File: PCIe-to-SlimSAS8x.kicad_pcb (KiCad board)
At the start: 4 copper layers, 27.3 x 51.3 mm, 11 parts, among them J1 PCI_Express_x8, J2 OpenCAPI_AAC_Host

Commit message: Initial Layout Complete
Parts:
- renumbered R4 to R3, R3 to R4
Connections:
- net PERn0 renamed Rx0_P
- net PERn1 renamed Rx1_P
- net PERn2 renamed Rx2_P
- net PERn3 renamed Rx3_P
- net PERn4 renamed Rx4_P
- net PERn5 renamed Rx5_P
- net PERn6 renamed Rx6_P
- net PERn7 renamed Rx7_P
- net PERp0 renamed Rx0_N
- net PERp1 renamed Rx1_N
- net PERp2 renamed Rx2_N
- net PERp3 renamed Rx3_N
- net PERp4 renamed Rx4_N
- net PERp5 renamed Rx5_N
- net PERp6 renamed Rx6_N
- net PERp7 renamed Rx7_N
- net REFCLKn renamed REFCLK_N
- net REFCLKp renamed REFCLK_P
- J1 pad B14: PETp0 -> Tx0_P
- J1 pad B15: PETn0 -> Tx0_N
- J1 pad B19: PETp1 -> Tx1_P
- J1 pad B20: PETn1 -> Tx1_N
- J1 pad B23: PETp2 -> Tx2_P
- J1 pad B24: PETn2 -> Tx2_N
- J1 pad B27: PETp3 -> Tx3_P
- J1 pad B28: PETn3 -> Tx3_N
- J1 pad B33: PETp4 -> Tx4_P
- J1 pad B34: PETn4 -> Tx4_N
- J1 pad B37: PETp5 -> Tx5_P
- J1 pad B38: PETn5 -> Tx5_N
- J1 pad B41: PETp6 -> Tx6_P
- J1 pad B42: PETn6 -> Tx6_N
- J1 pad B45: PETp7 -> Tx7_P
- J1 pad B46: PETn7 -> Tx7_N
- J2 pad A14: PETp5 -> Tx5_N
- J2 pad A15: PETn5 -> Tx5_P
- J2 pad A17: PETp7 -> Tx7_N
- J2 pad A18: PETn7 -> Tx7_P
- J2 pad A2: PETp0 -> Tx0_N
- J2 pad A3: PETn0 -> Tx0_P
- J2 pad A5: PETp2 -> Tx2_N
- J2 pad A6: PETn2 -> Tx2_P
- J2 pad B11: PETp4 -> Tx4_N
- J2 pad B12: PETn4 -> Tx4_P
- J2 pad B14: PETp6 -> Tx6_N
- J2 pad B15: PETn6 -> Tx6_P
- J2 pad B2: PETp1 -> Tx1_N
- J2 pad B3: PETn1 -> Tx1_P
- J2 pad B5: PETp3 -> Tx3_N
- J2 pad B6: PETn3 -> Tx3_P
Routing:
- net GND: track 18.1 -> 307.2 mm, vias 13 -> 143
- net nPERST: track 0.00 -> 69.5 mm, vias 0 -> 2
- net Tx7_N: track 0.00 -> 45.9 mm, vias 0 -> 1
- net REFCLK_N: track 16.0 -> 59.9 mm
- net Tx7_P: track 0.00 -> 43.5 mm, vias 0 -> 1
- net Tx5_N: track 0.00 -> 40.1 mm, vias 0 -> 3
- net Tx0_P: track 0.00 -> 37.6 mm, vias 0 -> 1
- net Tx5_P: track 0.00 -> 37.4 mm, vias 0 -> 3
- net Rx0_P: track 0.00 -> 37.3 mm, vias 0 -> 2
- net Rx0_N: track 0.00 -> 36.8 mm, vias 0 -> 2
- net Tx0_N: track 0.00 -> 36.8 mm, vias 0 -> 1
- net Tx2_N: track 0.00 -> 31.5 mm, vias 0 -> 1
- net Rx2_N: track 0.00 -> 30.7 mm, vias 0 -> 2
- net Rx2_P: track 0.00 -> 29.0 mm, vias 0 -> 2
- net Tx6_N: track 0.00 -> 28.4 mm, vias 0 -> 1
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- added copper zone on B.Cu, net GND
- added copper zone on F.Cu, net GND
- added copper zone on In1.Cu, net GND
- added copper zone on In2.Cu, net GND

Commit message: PCB Layout Complete
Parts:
- turned R3 to 0 degrees
- turned R4 to 0 degrees
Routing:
- net GND: track 307.2 -> 360.6 mm
- net Tx1_N: track 18.6 -> 36.2 mm
- net Tx1_P: track 19.0 -> 33.7 mm
- net Tx6_P: track 25.8 -> 37.0 mm
- net Tx6_N: track 28.4 -> 37.0 mm
- net Rx1_N: track 22.8 -> 30.5 mm
- net Rx1_P: track 22.8 -> 30.5 mm
- net Tx3_P: track 18.3 -> 24.8 mm
- net Tx2_P: track 28.2 -> 34.3 mm
- net Tx3_N: track 19.5 -> 24.9 mm
- net Tx0_P: track 37.6 -> 34.0 mm
- net Tx0_N: track 36.8 -> 33.2 mm
- net Tx2_N: track 31.5 -> 34.2 mm
- net Rx2_P: track 29.0 -> 31.7 mm
- net REFCLK_N: track 59.9 -> 62.4 mm
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
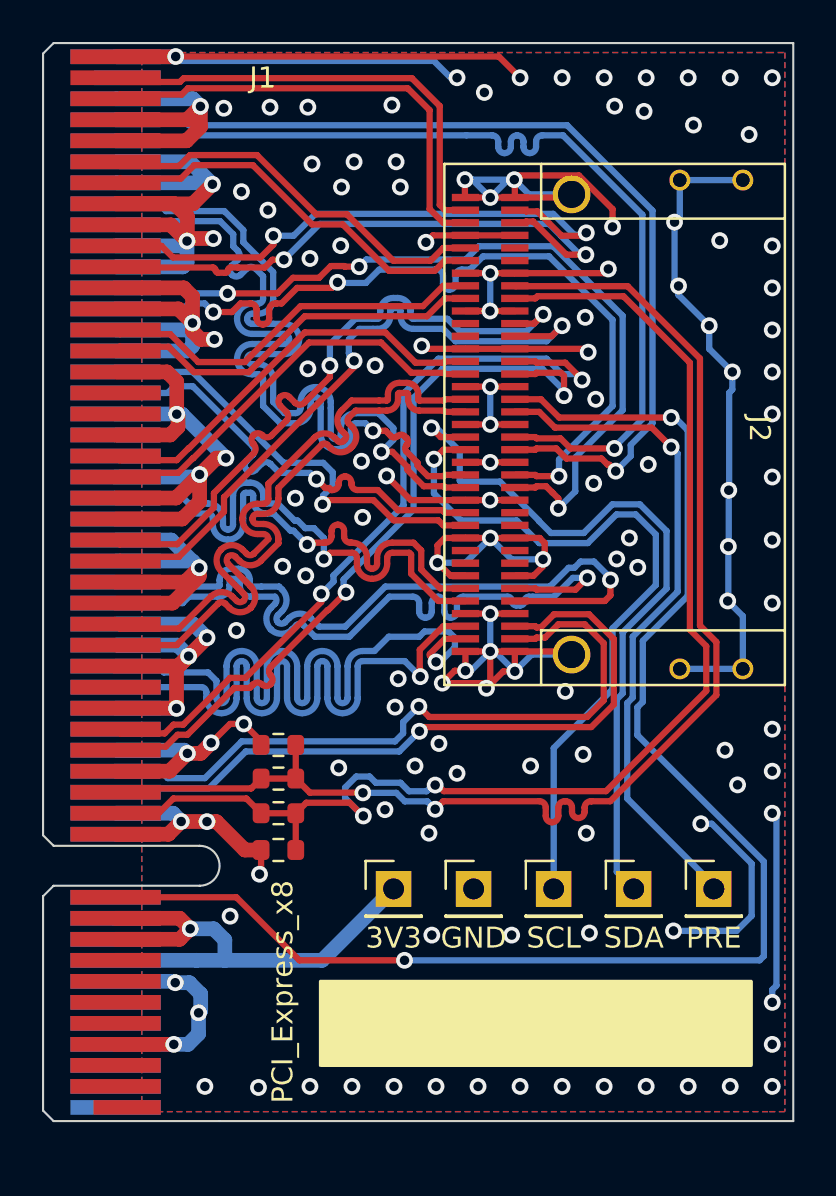
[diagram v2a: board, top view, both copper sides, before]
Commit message: Added Microstrip Test Trace
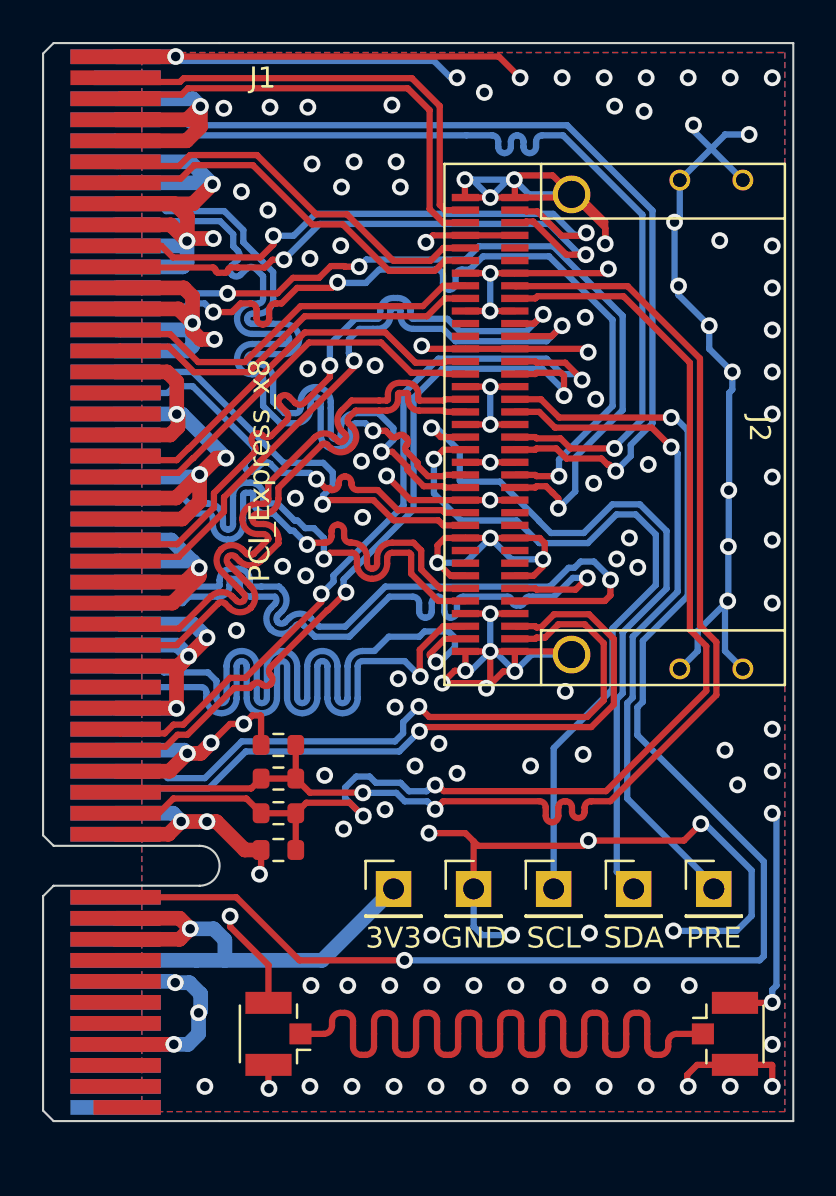
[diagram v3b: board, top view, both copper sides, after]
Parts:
- added J3: U.FL, Connector_Coaxial:U.FL_Hirose_U.FL-R-SMT-1_Vertical, F.Cu at (109.8, 108.5)
- added J4: U.FL, Connector_Coaxial:U.FL_Hirose_U.FL-R-SMT-1_Vertical, F.Cu at (88.5, 108.5)
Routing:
- net Net-(J3-Pad1): track 0.00 -> 44.8 mm
- net GND: track 360.6 -> 403.9 mm, vias 143 -> 154
